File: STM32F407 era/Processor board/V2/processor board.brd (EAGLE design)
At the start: 61.4 x 43.5 mm, 43 parts, among them IC1 REG1117, U2 MAX13052ESA+, X2 057-010-1, Y1 25 MHz, Y2 32.768KHz

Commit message: minor updates to board layout
Added USB power fuse, and added toggle switch for boot switch
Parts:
- removed S2: BOOT, SparkFun-Electromechanical:TACTILE-SWITCH-1101NE
- added U$32: SWITCH_SPDT, SparkFun-Electromechanical:KPS-1290
- moved PTC1 42.6 mm to (12.4, 40.0), turned to 180 degrees
- moved TP1 4.41 mm to (54.6, 7.91)
- moved R1 2.56 mm to (21.0, 18.7)
- moved R2 2.01 mm to (10.9, 20.1)
- moved C18 1.80 mm to (13.9, 42.0), turned to 180 degrees
- moved X1 1.27 mm to (4.70, 36.3)
- moved C16 1.13 mm to (10.9, 38.1), turned to 0 degrees
- moved C17 0.90 mm to (13.9, 38.3), turned to 0 degrees
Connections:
- new net N$7: C17.2, IC1.3, PTC1.1
- net 3.3V: now also U$32.O; no longer S2.2
- net N$4: now also U$32.P; no longer S2.1
- net USB_VBUS: now also PTC1.2; no longer C17.2, IC1.3
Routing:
- net N$7: track 0.00 -> 4.77 mm
- net USB_VBUS: track 8.32 -> 4.74 mm
- net GND: track 11.5 -> 14.2 mm, vias 18 -> 25
- net RESET: track 78.4 -> 80.8 mm
- net USB_DP: track 34.8 -> 36.1 mm
- net USB_DM: track 35.7 -> 37.0 mm
- net USB_ID: track 36.0 -> 37.2 mm
- net N$4: track 22.7 -> 23.7 mm

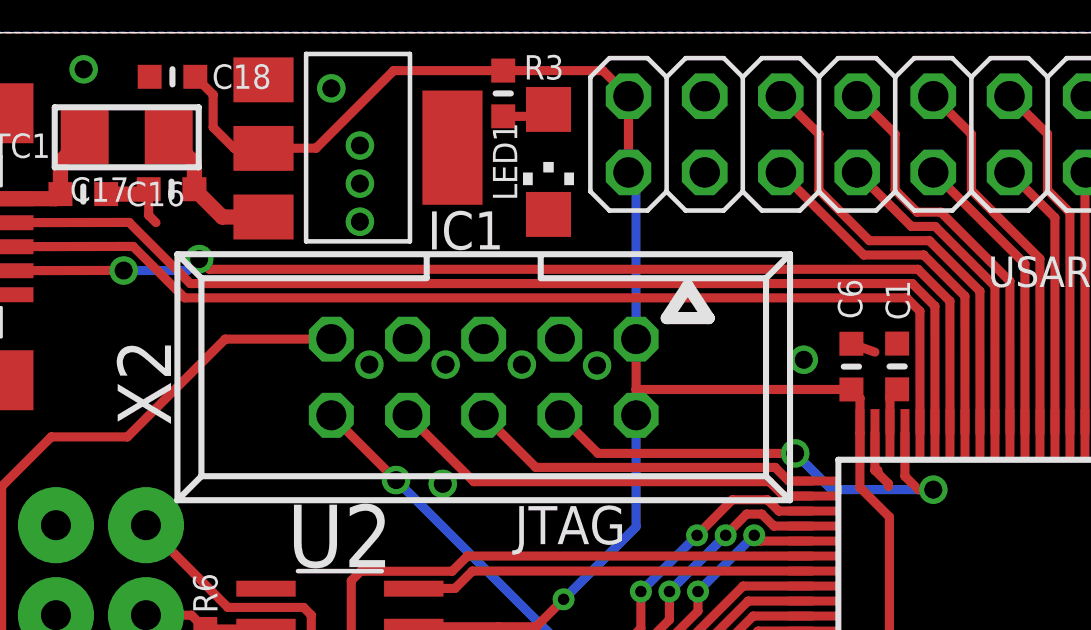
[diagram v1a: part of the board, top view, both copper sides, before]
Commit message: Added RPM leds and constant current IC's
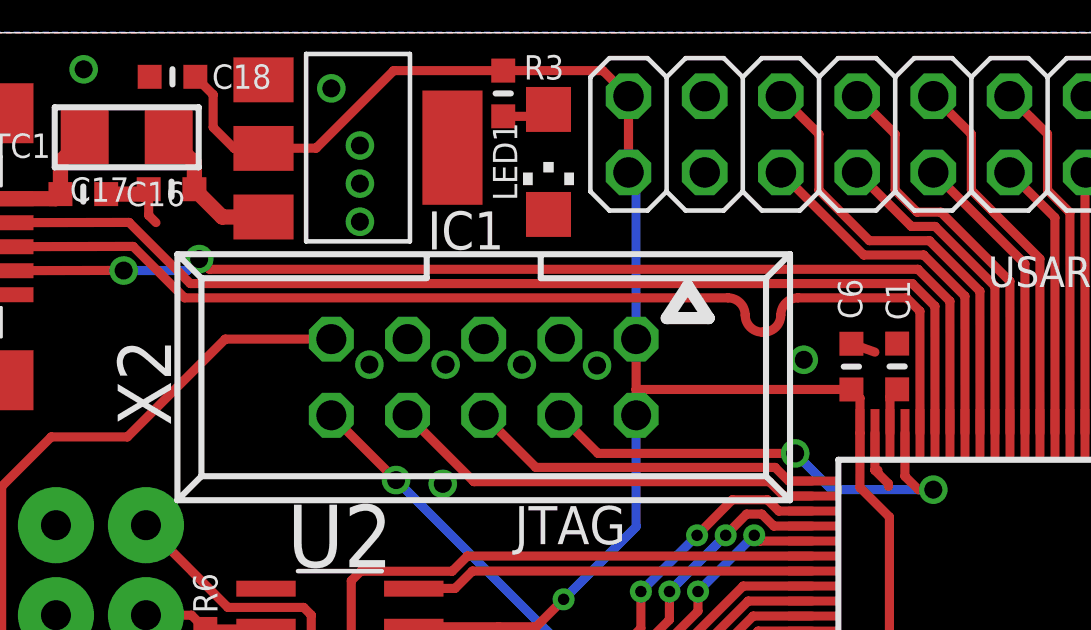
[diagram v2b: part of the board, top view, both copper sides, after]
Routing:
- net USB_DP: track 36.1 -> 37.0 mm
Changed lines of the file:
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@@
 <setting verticaltext="up"/>
 </settings>
-<grid distance="0.0125" unitdist="inch" unit="mil" style="lines" multiple="1" display="yes" altdistance="0.025" altunitdist="inch" altunit="inch"/>
+<grid distance="0.00125" unitdist="inch" unit="inch" style="lines" multiple="1" display="yes" altdistance="0.025" altunitdist="inch" altunit="inch"/>
 <layers>
 <layer number="1" name="Top" color="4" fill="1" visible="yes" active="yes"/>
@@
 <wire x1="38.799" y1="34.19425" x2="38.8011875" y2="30.132615625" width="0.3048" layer="1"/>
 <wire x1="12.573" y1="36.35375" x2="14.2875" y2="34.63925" width="0.3048" layer="1"/>
-<wire x1="14.2875" y1="34.63925" x2="38.354" y2="34.63925" width="0.3048" layer="1"/>
+<wire x1="14.2875" y1="34.63925" x2="32.402315625" y2="34.63925" width="0.3048" layer="1"/>
+<wire x1="32.402315625" y1="34.63925" x2="32.973815625" y2="34.06775" width="0.3048" layer="1" curve="-90"/>
+<wire x1="32.973815625" y1="34.06775" x2="33.545315625" y2="33.49625" width="0.3048" layer="1" curve="90"/>
+<wire x1="33.545315625" y1="33.49625" x2="33.5915" y2="33.49625" width="0.3048" layer="1"/>
+<wire x1="33.5915" y1="33.49625" x2="34.163" y2="34.06775" width="0.3048" layer="1" curve="90"/>
+<wire x1="34.163" y1="34.06775" x2="34.7345" y2="34.63925" width="0.3048" layer="1" curve="-90"/>
+<wire x1="34.7345" y1="34.63925" x2="38.354" y2="34.63925" width="0.3048" layer="1"/>
 </signal>
 <signal name="JTAG_TMS">

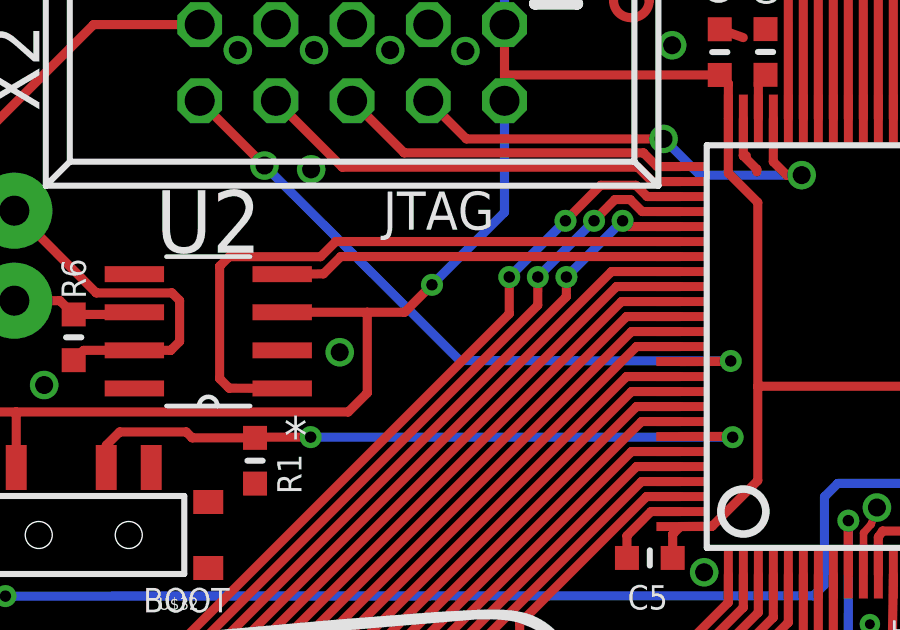
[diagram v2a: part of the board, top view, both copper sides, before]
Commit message: fixed CAN controller connections
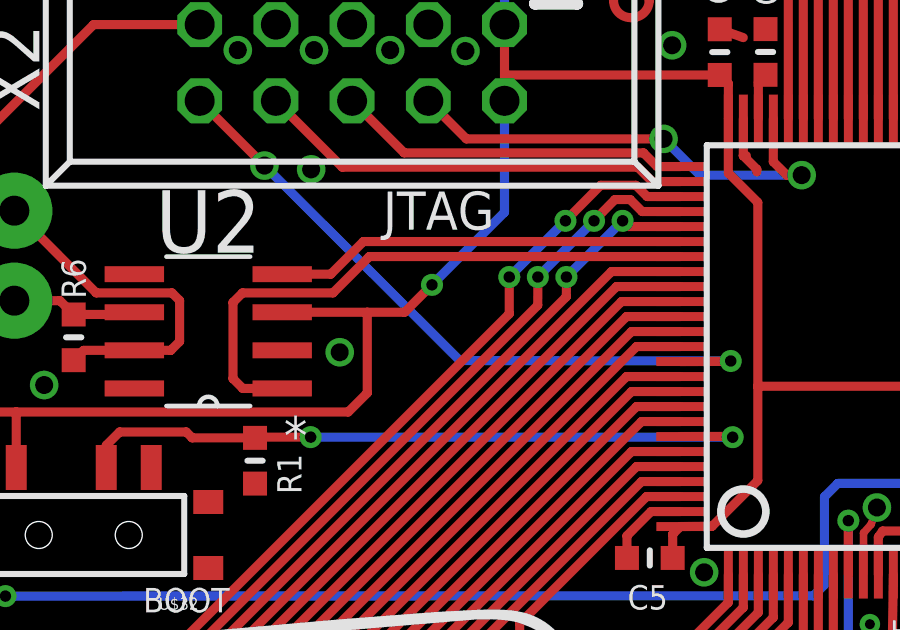
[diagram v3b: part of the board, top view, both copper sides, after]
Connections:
- net CAN_RX: now also U2.4; no longer U2.1
- net CAN_TX: now also U2.1; no longer U2.4
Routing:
- net CAN_RX: track 21.7 -> 13.7 mm
- net CAN_TX: track 13.5 -> 19.9 mm
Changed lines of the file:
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@@
 </signal>
 <signal name="CAN_RX">
-<contactref element="U2" pad="1"/>
 <contactref element="U1" pad="81"/>
-<wire x1="23.20925" y1="25.527" x2="20.16125" y2="25.527" width="0.3048" layer="1"/>
-<wire x1="20.16125" y1="25.527" x2="19.84375" y2="25.2095" width="0.3048" layer="1"/>
-<wire x1="19.84375" y1="25.2095" x2="19.84375" y2="21.463" width="0.3048" layer="1"/>
-<wire x1="19.84375" y1="21.463" x2="20.16125" y2="21.1455" width="0.3048" layer="1"/>
-<wire x1="20.16125" y1="21.1455" x2="21.9287375" y2="21.135615625" width="0.3048" layer="1"/>
-<wire x1="35.2011875" y1="26.032615625" x2="23.714865625" y2="26.032615625" width="0.3048" layer="1"/>
-<wire x1="23.714865625" y1="26.032615625" x2="23.20925" y2="25.527" width="0.3048" layer="1"/>
+<contactref element="U2" pad="4"/>
+<wire x1="35.2011875" y1="26.032615625" x2="24.635615625" y2="26.032615625" width="0.3048" layer="1"/>
+<wire x1="24.635615625" y1="26.032615625" x2="23.548615625" y2="24.945615625" width="0.3048" layer="1"/>
+<wire x1="23.548615625" y1="24.945615625" x2="21.9287375" y2="24.945615625" width="0.3048" layer="1"/>
 </signal>
 <signal name="CAN_TX">
-<contactref element="U2" pad="4"/>
 <contactref element="U1" pad="82"/>
-<wire x1="23.3045" y1="24.9555" x2="21.9287375" y2="24.945615625" width="0.3048" layer="1"/>
-<wire x1="35.2011875" y1="25.532615625" x2="23.881615625" y2="25.532615625" width="0.3048" layer="1"/>
-<wire x1="23.881615625" y1="25.532615625" x2="23.3045" y2="24.9555" width="0.3048" layer="1"/>
+<contactref element="U2" pad="1"/>
+<wire x1="35.2011875" y1="25.532615625" x2="24.834115625" y2="25.532615625" width="0.3048" layer="1"/>
+<wire x1="24.834115625" y1="25.532615625" x2="23.622" y2="24.3205" width="0.3048" layer="1"/>
+<wire x1="23.622" y1="24.3205" x2="20.60575" y2="24.3205" width="0.3048" layer="1"/>
+<wire x1="20.60575" y1="24.3205" x2="20.28825" y2="24.003" width="0.3048" layer="1"/>
+<wire x1="20.28825" y1="24.003" x2="20.28825" y2="21.463" width="0.3048" layer="1"/>
+<wire x1="20.28825" y1="21.463" x2="20.615634375" y2="21.135615625" width="0.3048" layer="1"/>
+<wire x1="20.615634375" y1="21.135615625" x2="21.9287375" y2="21.135615625" width="0.3048" layer="1"/>
 </signal>
 <signal name="RESET">

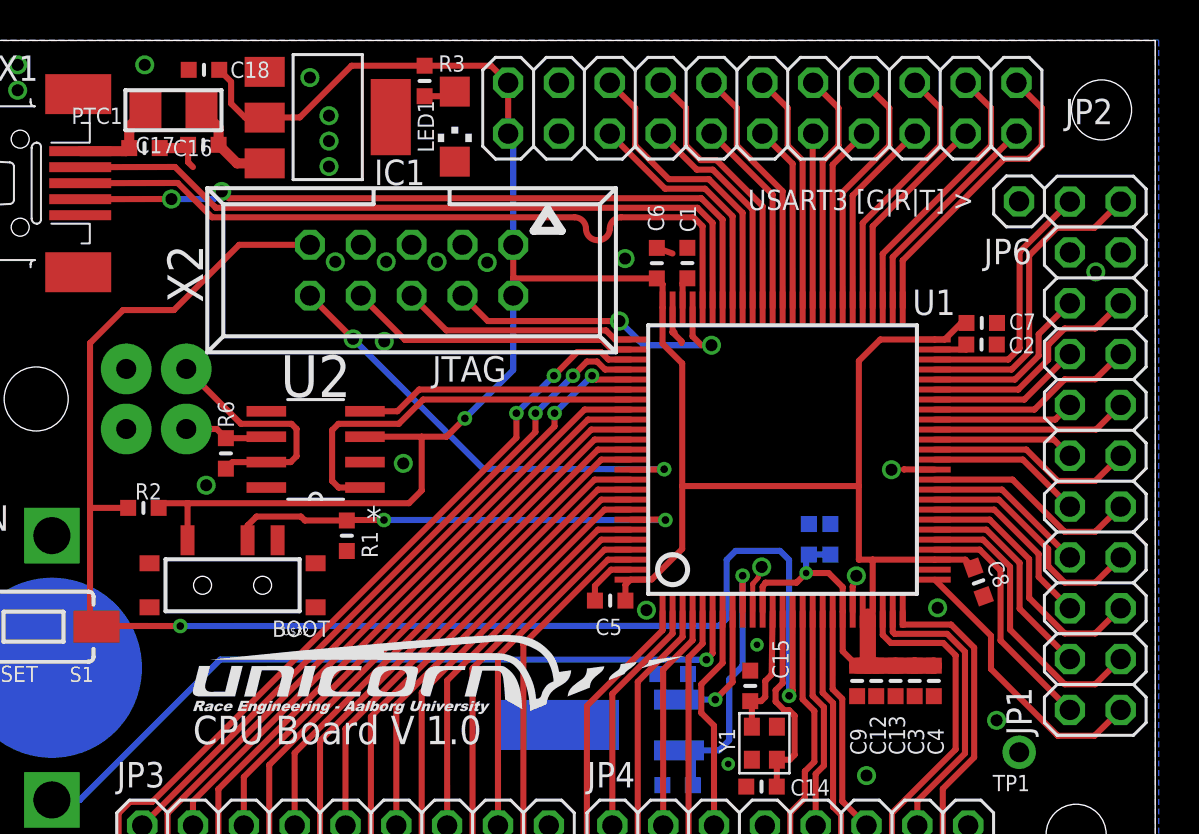
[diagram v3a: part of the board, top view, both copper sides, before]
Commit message: minor changes to layout
Fixed impendance circuit for the CAN transciever
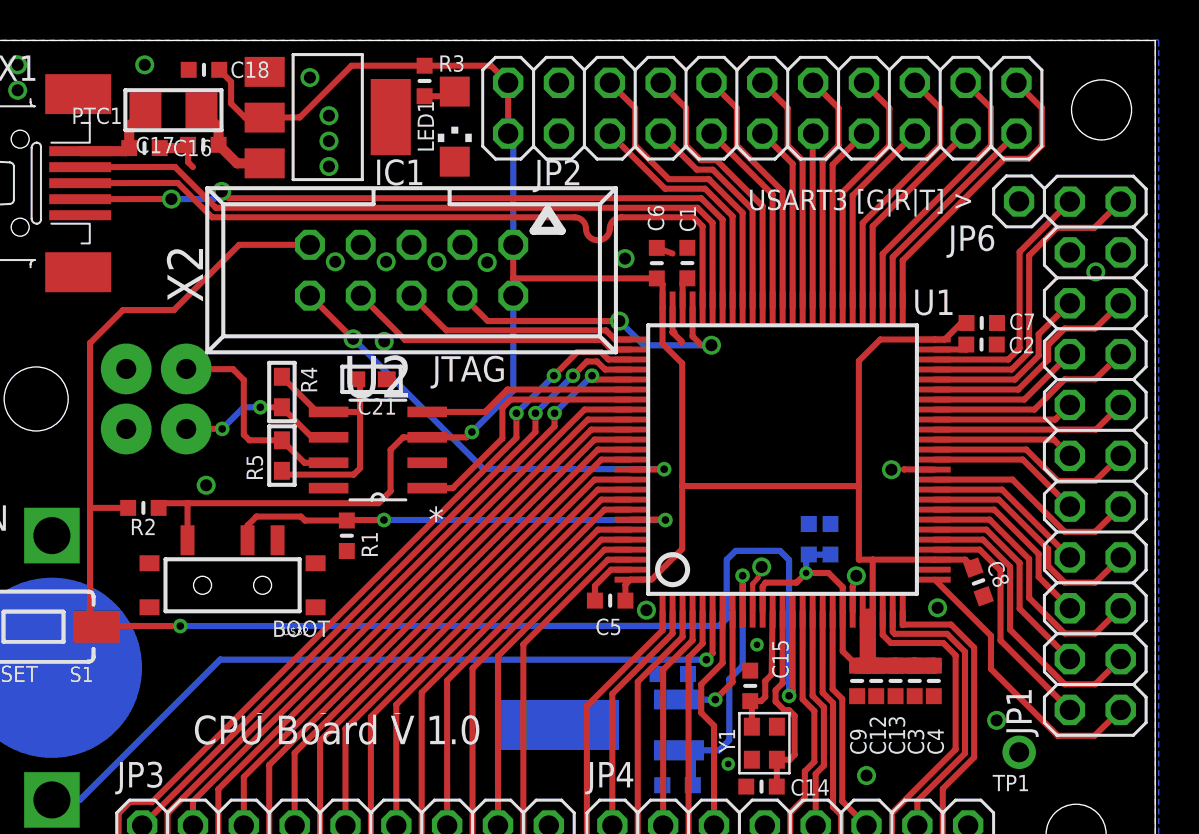
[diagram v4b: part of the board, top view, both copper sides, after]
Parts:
- removed R6: 1k8, microbuilder:_0603MP
- added C21: 4n7, microbuilder:_0603
- added R4, R5: 60, microbuilder:_0603
- moved U2 3.11 mm to (22.6, 23.0)
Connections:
- new net N$8: C21.2, R4.1, R5.1, U2.5
- net CANH: now also R5.2; no longer R6.1
- net CANL: now also R4.2; no longer R6.2
- net GND: now also C21.1
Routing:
- net N$8: track 0.00 -> 13.3 mm
- net CAN_TX: track 19.9 -> 12.9 mm
- net CANL: track 4.22 -> 8.18 mm, vias 0 -> 2
- net CAN_RX: track 13.7 -> 10.6 mm
- net 3.3V: track 137.4 -> 134.8 mm
- net CANH: track 11.9 -> 10.7 mm
- net GND: vias 25 -> 24

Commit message: minor changes to layout
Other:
- board text added: "CPU Board V 2.0"
- board text removed: "CPU Board V 1.0"
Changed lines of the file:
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@@
 Peter Reichwald</text>
 <text x="41.06418125" y="35.0012" size="1.016" layer="25">USART3 [G|R|T] &gt;</text>
-<rectangle x1="16.635734375" y1="9.813290625" x2="16.696696875" y2="9.820909375" layer="25"/>
-<rectangle x1="19.80565625" y1="9.813290625" x2="19.8666125" y2="9.820909375" layer="25"/>
-<rectangle x1="23.524215625" y1="9.813290625" x2="23.585171875" y2="9.820909375" layer="25"/>
-<rectangle x1="16.582396875" y1="9.820909375" x2="16.757653125" y2="9.828528125" layer="25"/>
-<rectangle x1="19.744696875" y1="9.820909375" x2="19.919953125" y2="9.828528125" layer="25"/>
-<rectangle x1="23.46325625" y1="9.820909375" x2="23.6385125" y2="9.828528125" layer="25"/>
-<rectangle x1="16.559534375" y1="9.828528125" x2="16.788134375" y2="9.836146875" layer="25"/>
-<rectangle x1="19.721834375" y1="9.828528125" x2="19.950434375" y2="9.836146875" layer="25"/>
-<rectangle x1="23.440396875" y1="9.828528125" x2="23.668996875" y2="9.836146875" layer="25"/>
-<rectangle x1="16.544296875" y1="9.83615" x2="16.803371875" y2="9.84376875" layer="25"/>
-<rectangle x1="19.706596875" y1="9.83615" x2="19.973296875" y2="9.84376875" layer="25"/>
-<rectangle x1="23.42515625" y1="9.83615" x2="23.69185625" y2="9.84376875" layer="25"/>
-<rectangle x1="16.52905625" y1="9.84376875" x2="16.8186125" y2="9.8513875" layer="25"/>
-<rectangle x1="19.698975" y1="9.84376875" x2="19.98853125" y2="9.8513875" layer="25"/>
-<rectangle x1="23.417534375" y1="9.84376875" x2="23.707096875" y2="9.8513875" layer="25"/>
-<rectangle x1="16.521434375" y1="9.851390625" x2="16.833853125" y2="9.859009375" layer="25"/>
-<rectangle x1="19.69135625" y1="9.851390625" x2="20.003775" y2="9.859009375" layer="25"/>
-<rectangle x1="23.409915625" y1="9.851390625" x2="23.722334375" y2="9.859009375" layer="25"/>
-<rectangle x1="16.521434375" y1="9.859009375" x2="16.849096875" y2="9.866628125" layer="25"/>
-<rectangle x1="19.683734375" y1="9.859009375" x2="20.011396875" y2="9.866628125" layer="25"/>
-<rectangle x1="23.402296875" y1="9.859009375" x2="23.729953125" y2="9.866628125" layer="25"/>
-<text x="13.332459375" y="9.733278125" size="1.4224" layer="25" align="top-left">CPU Board V 1.0</text>
+<text x="13.332459375" y="9.733278125" size="1.4224" layer="25" align="top-left">CPU Board V 2.0</text>
 <hole x="57.4675" y="3.81" drill="3"/>
 <hole x="58.7375" y="40.005" drill="3"/>
@@
 <attribute name="MF" value="" x="4.7011875" y="36.343865625" size="1.778" layer="27" display="off"/>
 <attribute name="OC_FARNELL" value="unknown" x="4.7011875" y="36.343865625" size="1.778" layer="27" display="off"/>
-<attribute name="NAME" x="3.5327875" y="41.456884375" size="1.27" layer="25"/>
+<attribute name="NAME" x="3.4057875" y="30.471384375" size="1.27" layer="25"/>
 <attribute name="VALUE" x="0.2561875" y="29.358865625" size="1.27" layer="27"/>
 </element>
 <element name="C16" library="microbuilder" package="_0603MP" value="4u7" x="10.912115625" y="38.0978125" smashed="yes">
-<attribute name="NAME" x="12.329434375" y="37.696490625" size="0.8128" layer="25" ratio="18"/>
-<attribute name="VALUE" x="9.959615625" y="37.1453125" size="0.4064" layer="27" ratio="10"/>
+<attribute name="NAME" x="9.852934375" y="36.775740625" size="0.8128" layer="25" ratio="18"/>
+<attribute name="VALUE" x="9.5589375" y="37.645615625" size="0.4064" layer="27" ratio="10" rot="R90"/>
 </element>
 <element name="BAT1" library="SparkFun-Electromechanical" package="BATTCON_12MM_PTH" value="CR1220" x="6.2865" y="12.1285" smashed="yes" rot="MR270">
@@
 </element>
 <element name="C17" library="microbuilder" package="_0603MP" value="10u" x="13.852884375" y="38.2609375" smashed="yes">
-<attribute name="NAME" x="12.438659375" y="38.655346875" size="0.8128" layer="25" ratio="18" rot="R180"/>
-<attribute name="VALUE" x="12.900384375" y="37.3084375" size="0.4064" layer="27" ratio="10"/>
+<attribute name="NAME" x="12.929590625" y="36.909653125" size="0.8128" layer="25" ratio="18"/>
+<attribute name="VALUE" x="12.6025625" y="37.760634375" size="0.4064" layer="27" ratio="10" rot="R90"/>
 </element>
 <element name="C18" library="microbuilder" package="_0603MP" value="22u" x="13.884634375" y="42.0074375" smashed="yes" rot="R180">
-<attribute name="NAME" x="15.20090625" y="41.606821875" size="0.8128" layer="25" ratio="18"/>
+<attribute name="NAME" x="12.272928125" y="41.07715625" size="0.8128" layer="25" ratio="18" rot="R90"/>
 <attribute name="VALUE" x="14.837134375" y="42.9599375" size="0.4064" layer="27" ratio="10" rot="R180"/>
 </element>
@@
 <attribute name="VALUE" x="57.79008125" y="34.163" size="1.27" layer="27" rot="R90"/>
 </element>
-<element name="PTC1" library="microbuilder" package="1206" value="" x="12.359640625" y="39.989759375" rot="R180"/>
+<element name="PTC1" library="microbuilder" package="1206" value="" x="12.359640625" y="39.989759375" smashed="yes" rot="R180">
+<attribute name="NAME" x="7.166609375" y="42.210990625" size="0.8128" layer="25" ratio="18"/>
+<attribute name="VALUE" x="9.819640625" y="40.624759375" size="0.4064" layer="27" ratio="10" rot="R180"/>
+</element>
 <element name="U$32" library="SparkFun-Electromechanical" package="KPS-1290" value="SWITCH_SPDT" x="15.313659375" y="16.25091875">
 <attribute name="PROD_ID" value="SWCH-10651" x="15.313659375" y="16.25091875" size="1.778" layer="27" display="off"/>

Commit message: more final board prepping for production
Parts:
- moved C10 59.7 mm to (103.8, 18.9)
- moved C11 59.7 mm to (104.9, 18.9)
- moved C12 59.7 mm to (107.2, 11.8)
- moved C13 59.7 mm to (108.1, 11.8)
- moved C18 59.7 mm to (73.6, 42.3)
- moved C19 59.7 mm to (97.0, 12.1)
- moved C2 59.7 mm to (112.4, 28.6)
- moved C3 59.7 mm to (109.1, 11.8)
- moved C7 59.7 mm to (112.4, 29.7)
- moved C9 59.7 mm to (106.2, 11.8)
- moved IC1 59.7 mm to (79.8, 40.0)
- moved JP1 59.7 mm to (118.1, 23.0)
- moved JP2 59.7 mm to (101.5, 40.4)
- moved BAT1 59.7 mm to (66.0, 12.4)
- moved C1 59.7 mm to (97.7, 32.7)
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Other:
- board text removed: "Henrik Jensen Jakob Jensen JesperJørgensen Peter Reichwald"
